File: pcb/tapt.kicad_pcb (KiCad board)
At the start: 4 copper layers, 28.3 x 28.3 mm, 38 parts, among them J1 Conn_01x05_Pin, J2 Conn_01x04_MountingPin, SW1 SW_SPDT_LIMIT, SW2 SW_SPST, U1 nRF52810-QCxx, Y1 32MHz, Y2 32.768kHz

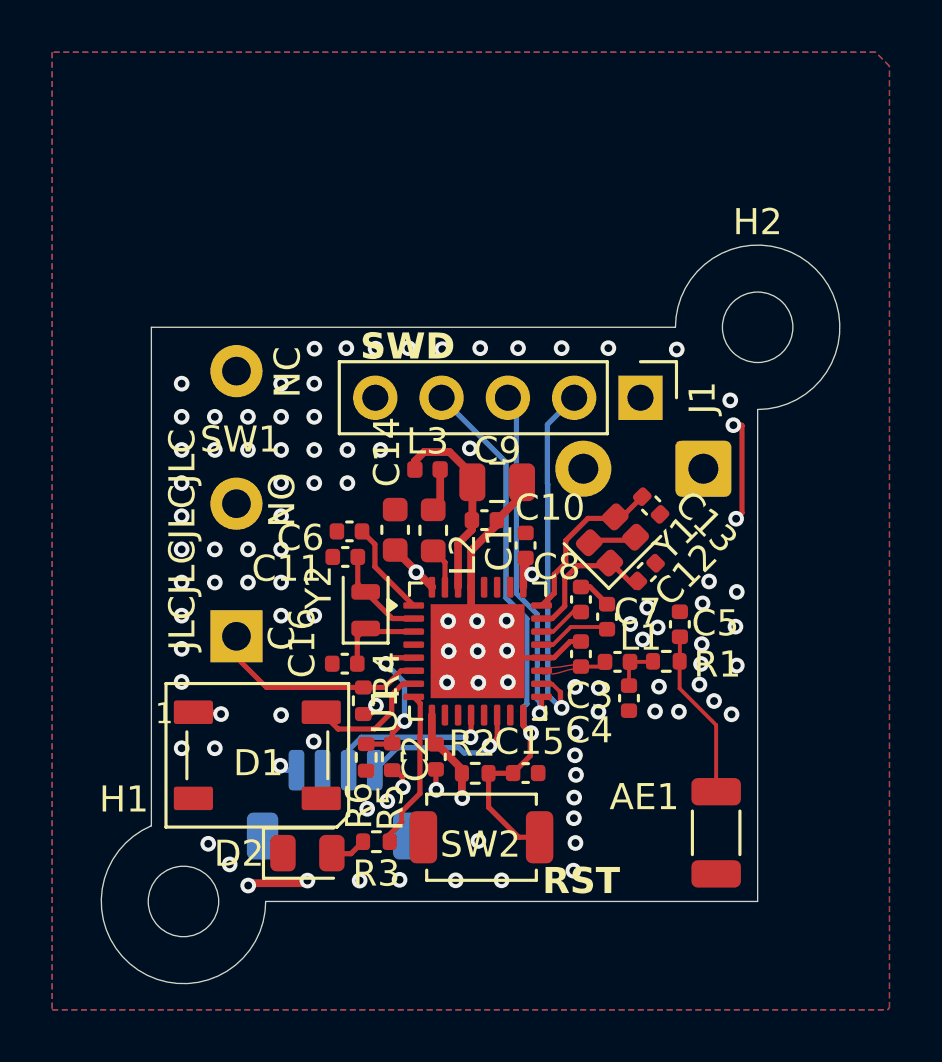
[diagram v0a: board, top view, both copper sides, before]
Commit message: pcb: voltage divider, antenna t-network
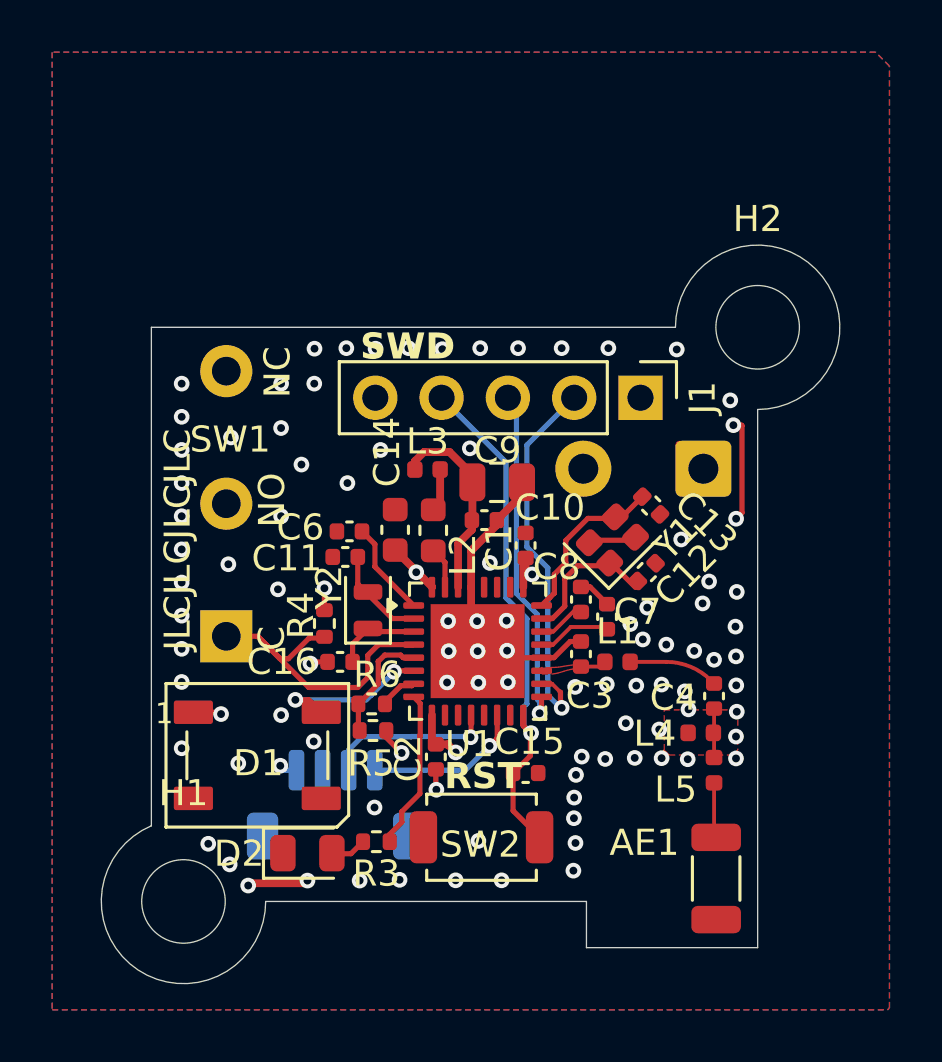
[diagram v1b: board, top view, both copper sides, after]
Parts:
- removed C5: 1pF, Capacitor_SMD:C_0402_1005Metric
- removed R1: 0, Resistor_SMD:R_0402_1005Metric
- removed R2: 100k, Resistor_SMD:R_0402_1005Metric
- added L4: 2.7nH, Inductor_SMD:L_0402_1005Metric, F.Cu at (106.7, 76.0)
- added L5: 3.9nH, Inductor_SMD:L_0402_1005Metric, F.Cu at (107.2, 77.4)
- C4: value 1pF -> 1.0pF
- H1, H2: footprint MountingHole:MountingHole_2.7mm_M2.5 -> MountingHole:MountingHole_3.2mm_M3
- L1: footprint Capacitor_SMD:C_0402_1005Metric -> Inductor_SMD:L_0402_1005Metric
- moved R4 3.31 mm to (92.2, 71.8), turned to 90 degrees
- moved C4 3.26 mm to (107.2, 74.6)
- moved R6 2.06 mm to (94.0, 74.9), turned to 0 degrees
- moved AE1 1.75 mm to (107.2, 81.6)
- moved R5 1.25 mm to (94.1, 75.9), turned to 180 degrees
- moved SW1 0.39 mm to (88.5, 72.3)
- moved C16 0.19 mm to (92.8, 73.3)
- moved Y2 0.09 mm to (93.9, 71.3)
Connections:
- C4 pad 2: GND -> Net-(C4-Pad2)
- R6 pad 2: GND -> BAT_MEASURE_GND
- U1 pad 4: unconnected-(U1-P0.04/AIN2-Pad4) -> LIMIT
- U1 pad 6: LIMIT -> NEOPIXEL
- U1 pad 7: NEOPIXEL -> BAT_MEASURE_GND
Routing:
- net Net-(AE1-FEED): track 6.50 -> 2.12 mm
- net LIMIT: track 8.34 -> 12.4 mm
- net Net-(C4-Pad2): track 0.00 -> 1.88 mm
- net RST: track 22.4 -> 20.7 mm
- net Net-(C4-Pad1): track 1.73 -> 3.44 mm
- net BAT_MEASURE_GND: track 0.00 -> 1.47 mm
- net NEOPIXEL: track 4.91 -> 6.20 mm, vias 0 -> 2
- net BAT_MEASURE: track 5.72 -> 4.48 mm, vias 2 -> 0
- net VDD: track 12.0 -> 10.9 mm
- net GND: track 21.1 -> 21.8 mm, vias 100 -> 94
- net SWDIO: track 14.0 -> 14.7 mm
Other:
- outline, holes or cut-outs redrawn

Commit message: pcb: minor rf routing improvements
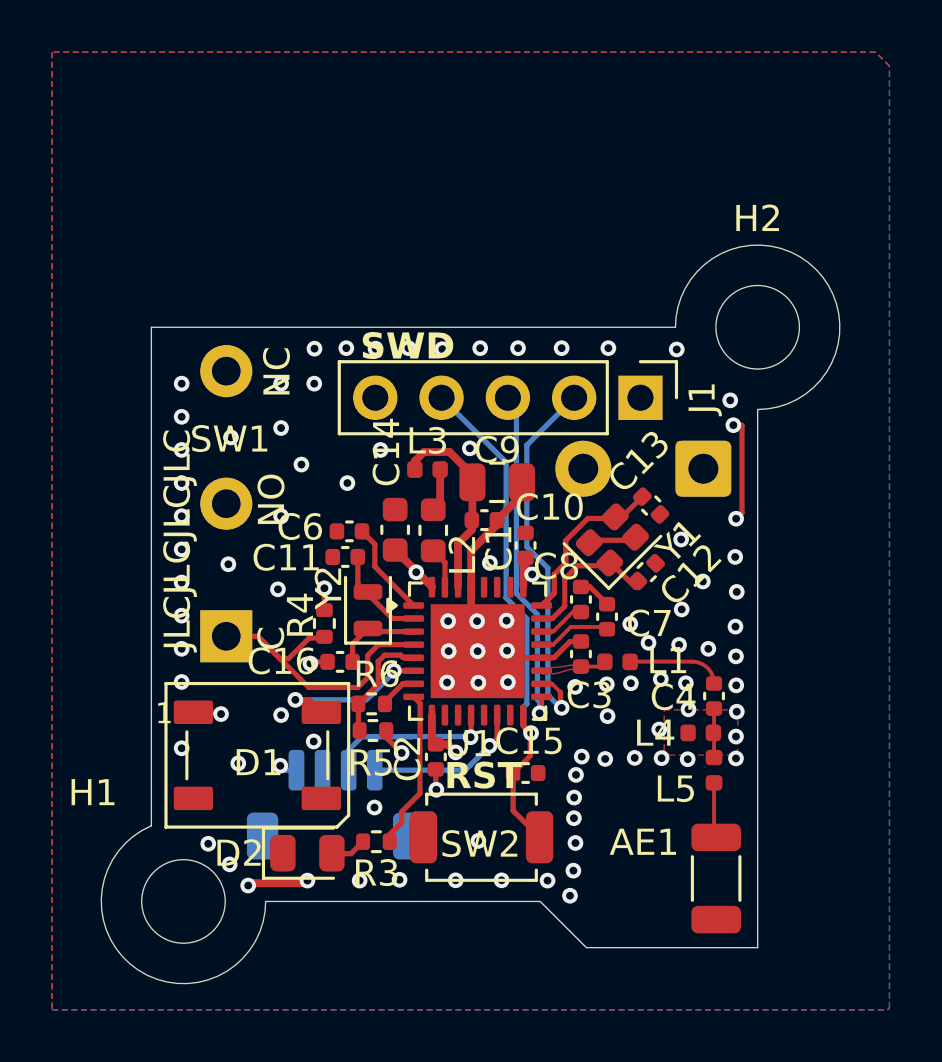
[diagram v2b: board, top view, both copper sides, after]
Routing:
- net GND: vias 94 -> 95
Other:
- outline, holes or cut-outs redrawn
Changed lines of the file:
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@@
 		(tags "capacitor")
 		(property "Reference" "C13"
-			(at -1.937473 1.046518 135)
+			(at 1.513209 0.86267 225)
 			(layer "F.SilkS")
 			(effects
@@
 		(tags "capacitor")
 		(property "Reference" "C7"
-			(at -0.19 -1.17 0)
+			(at 0.28 -1.64 0)
 			(layer "F.SilkS")
 			(effects
@@
 		(tags "inductor")
 		(property "Reference" "L1"
-			(at 0 -1.17 0)
+			(at 1.94 -0.03 0)
 			(layer "F.SilkS")
 			(effects
@@
 		(tags "mountinghole M3")
 		(property "Reference" "H1"
-			(at 0 -4.15 0)
+			(at -3.47 -4.15 0)
 			(layer "F.SilkS")
 			(effects
@@
 		(descr "SMD2016/4, Crystal, 2.0x1.6mm package, SMD, generated with kicad-footprint-generator make_crystal.py, http://www.q-crystal.com/upload/5/2015552223166229.pdf")
 		(property "Reference" "Y1"
-			(at 1.781945 1.674299 45)
+			(at 1.784691 1.841259 45)
 			(layer "F.SilkS")
 			(effects
@@
 		(tags "capacitor")
 		(property "Reference" "C12"
-			(at -0.989949 -1.131371 225)
+			(at -1.1243 -1.265721 225)
 			(layer "F.SilkS")
 			(effects
@@
 	)
 	(gr_line
-		(start 102.27 82.46)
+		(start 100.5 82.46)
 		(end 89.979937 82.46)
 		(stroke
@@
 	)
 	(gr_line
-		(start 102.27 82.46)
+		(start 100.5 82.46)
 		(end 102.27 84.23)
 		(stroke
@@
 	)
 	(via
-		(at 107.16 73.2)
-		(size 0.6)
-		(drill 0.3)
-		(layers "F.Cu" "B.Cu")
-		(free yes)
-		(net 3)
-	)
-	(via
 		(at 98.1 72.87)
 		(size 0.6)
@@
 	)
 	(via
-		(at 106.4 72.86)
-		(size 0.6)
-		(drill 0.3)
-		(layers "F.Cu" "B.Cu")
-		(free yes)
-		(net 3)
-	)
-	(via
-		(at 104.6 71.2)
+		(at 105.92 71.27)
 		(size 0.6)
 		(drill 0.3)
@@
 	)
 	(via
+		(at 101.64 82.24)
+		(size 0.6)
+		(drill 0.3)
+		(layers "F.Cu" "B.Cu")
+		(free yes)
+		(net 3)
+	)
+	(via
 		(at 86.76119 70.24)
 		(size 0.6)
@@
 	)
 	(via
+		(at 100.78 81.66)
+		(size 0.6)
+		(drill 0.3)
+		(layers "F.Cu" "B.Cu")
+		(free yes)
+		(net 3)
+	)
+	(via
 		(at 101.85 80.22)
 		(size 0.6)
@@
 	)
 	(via
+		(at 105.82 72.63)
+		(size 0.6)
+		(drill 0.3)
+		(layers "F.Cu" "B.Cu")
+		(free yes)
+		(net 3)
+	)
+	(via
 		(at 91.694265 73.344265)
 		(size 0.6)
@@
 	)
 	(via
-		(at 105.33 72.62)
-		(size 0.6)
-		(drill 0.3)
-		(layers "F.Cu" "B.Cu")
-		(free yes)
-		(net 3)
-	)
-	(via
 		(at 101.87 77.61)
 		(size 0.6)
@@
 	)
 	(via
-		(at 106.97 70.2)
+		(at 107.97 69.26)
 		(size 0.6)
 		(drill 0.3)
@@
 	)
 	(via
-		(at 106.04 74.41)
+		(at 106.08 74.1)
 		(size 0.6)
 		(drill 0.3)
@@
 	)
 	(via
-		(at 104.43 72.42)
+		(at 104.65 72.55)
 		(size 0.6)
 		(drill 0.3)
@@
 	)
 	(via
-		(at 103.78 75.63)
+		(at 103.08 75.36)
 		(size 0.6)
 		(drill 0.3)
@@
 	)
 	(via
-		(at 104.18 74.19)
+		(at 103.972917 74.1)
 		(size 0.6)
 		(drill 0.3)
@@
 	)
 	(via
-		(at 106.72 71.04)
+		(at 106.73 70.2)
 		(size 0.6)
 		(drill 0.3)
@@
 	)
 	(via
+		(at 106.94 72.78)
+		(size 0.6)
+		(drill 0.3)
+		(layers "F.Cu" "B.Cu")
+		(free yes)
+		(net 3)
+	)
+	(via
 		(at 108.01 74.18)
 		(size 0.6)
@@
 	)
 	(via
-		(at 105.15 74.15)
+		(at 105.12 73.94)
 		(size 0.6)
 		(drill 0.3)
@@
 	)
 	(segment
-		(start 105.33 73.28)
-		(end 103.945 73.28)
+		(start 103.945 73.28)
+		(end 103.955 73.27)
+		(width 0.1483)
+		(layer "F.Cu")
+		(net 6)
+	)
+	(segment
+		(start 107.16 74.11)
+		(end 107.16 74.11)
+		(width 0.1483)
+		(layer "F.Cu")
+		(net 6)
+	)
+	(segment
+		(start 106.32 73.27)
+		(end 103.955 73.27)
 		(width 0.1483)
 		(layer "F.Cu")
@@
 	)
 	(arc
-		(start 105.33 73.28)
-		(mid 106.253878 73.46377)
-		(end 107.037105 73.987106)
+		(start 107.16 74.11)
+		(mid 106.913969 73.51603)
+		(end 106.32 73.27)
 		(width 0.1483)
 		(layer "F.Cu")
@@
 	)
 	(segment
-		(start 95.65 73.62)
+		(start 94.928279 73.621)
 		(end 94.929279 73.62)
 		(width 0.2)
@@
 	)
 	(segment
+		(start 94.892 73.621)
+		(end 94.928279 73.621)
+		(width 0.2)
+		(layer "F.Cu")
+		(net 13)
+	)
+	(segment
 		(start 91.117573 74.735646)
 		(end 91.635646 74.735646)
@@
 	)
 	(segment
-		(start 91.635646 74.735646)
-		(end 92.11 75.21)
+		(start 94.929279 73.62)
+		(end 95.65 73.62)
 		(width 0.2)
 		(layer "F.Cu")
@@
 	)
 	(segment
-		(start 94.929279 73.62)
-		(end 94.891999 73.65728)
+		(start 91.635646 74.735646)
+		(end 92.11 75.21)
 		(width 0.2)
 		(layer "F.Cu")
@@
 	)
 	(via
-		(at 94.891999 73.65728)
+		(at 94.892 73.621)
 		(size 0.6)
 		(drill 0.3)
@@
 	)
 	(segment
-		(start 91.117573 74.735646)
-		(end 93.834536 74.735646)
+		(start 93.834536 74.735646)
+		(end 91.117573 74.735646)
 		(width 0.2)
 		(layer "B.Cu")
@@
 	(segment
 		(start 94.017616 74.56)
-		(end 94.891999 73.685617)
+		(end 94.010182 74.56)
 		(width 0.2)
 		(layer "B.Cu")
@@
 	)
 	(segment
-		(start 94.010182 74.56)
-		(end 94.017616 74.56)
+		(start 94.892 73.621)
+		(end 94.891999 73.621001)
 		(width 0.2)
 		(layer "B.Cu")
@@
 	(segment
 		(start 94.891999 73.685617)
-		(end 94.891999 73.65728)
+		(end 94.017616 74.56)
 		(width 0.2)
 		(layer "B.Cu")
@@
 	)
 	(segment
-		(start 93.834536 74.735646)
-		(end 94.010182 74.56)
+		(start 94.891999 73.621001)
+		(end 94.891999 73.685617)
+		(width 0.2)
+		(layer "B.Cu")
+		(net 13)
+	)
+	(segment
+		(start 94.010182 74.56)
+		(end 93.834536 74.735646)
 		(width 0.2)
 		(layer "B.Cu")
@@
 	)
 	(segment
-		(start 95.160202 74.194)
-		(end 95.576 74.194)
-		(width 0.2)
-		(layer "F.Cu")
-		(net 36)
-	)
-	(segment
 		(start 94.55 74.804202)
-		(end 95.160202 74.194)
+		(end 94.55 74.89)
 		(width 0.2)
 		(layer "F.Cu")
@@
 	)
 	(segment
-		(start 94.55 74.89)
+		(start 95.234202 74.12)
 		(end 94.55 74.804202)
 		(width 0.2)
@@
 	)
 	(segment
-		(start 95.576 74.194)
-		(end 95.65 74.12)
+		(start 95.65 74.12)
+		(end 95.234202 74.12)
 		(width 0.2)
 		(layer "F.Cu")

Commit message: chore: production files, bom, readme updates
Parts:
- moved L1 0.18 mm to (103.5, 73.1)
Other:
- board text added: "Stackup: JLC04161H-7628"
- board text removed: "Stackup: JLC04161H-3313"
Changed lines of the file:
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@@
 	(footprint "Inductor_SMD:L_0402_1005Metric"
 		(layer "F.Cu")
-		(at 103.46 73.28)
+		(at 103.46 73.1)
 		(descr "Inductor SMD 0402 (1005 Metric), square (rectangular) end terminal, IPC-7351 nominal, (Body size source: http://www.tortai-tech.com/upload/download/2011102023233369053.pdf), generated with kicad-footprint-generator")
 		(tags "inductor")
@@
 		)
 	)
-	(gr_text "Stackup: JLC04161H-3313"
+	(gr_text "Stackup: JLC04161H-7628"
 		(at 81.56 48.77 0)
 		(layer "Cmts.User")
@@
 	)
 	(segment
-		(start 107.24 80.005)
+		(start 107.16 77.915)
 		(end 107.16 79.925)
-		(width 0.1483)
+		(width 0.2939)
 		(layer "F.Cu")
 		(net 1)
@@
 	(segment
 		(start 107.16 79.925)
-		(end 107.16 77.915)
-		(width 0.1483)
+		(end 107.24 80.005)
+		(width 0.2939)
 		(layer "F.Cu")
 		(net 1)
@@
 	)
 	(via
-		(at 100.78 81.66)
+		(at 107.01 72.59)
 		(size 0.6)
 		(drill 0.3)
@@
 	)
 	(via
-		(at 101.85 80.22)
+		(at 106.04 72.39)
 		(size 0.6)
 		(drill 0.3)
@@
 	)
 	(via
-		(at 95.11 81.63)
+		(at 100.78 81.66)
 		(size 0.6)
 		(drill 0.3)
@@
 	)
 	(via
-		(at 90.57 64.32)
+		(at 101.85 80.22)
 		(size 0.6)
 		(drill 0.3)
@@
 	)
 	(via
-		(at 102.99 77)
+		(at 95.11 81.63)
 		(size 0.6)
 		(drill 0.3)
@@
 	)
 	(via
-		(at 105.82 72.63)
+		(at 90.57 64.32)
+		(size 0.6)
+		(drill 0.3)
+		(layers "F.Cu" "B.Cu")
+		(free yes)
+		(net 3)
+	)
+	(via
+		(at 102.99 77)
 		(size 0.6)
 		(drill 0.3)
@@
 	)
 	(via
-		(at 106.08 74.1)
+		(at 106.29 74.16)
 		(size 0.6)
 		(drill 0.3)
@@
 	)
 	(via
-		(at 104.65 72.55)
-		(size 0.6)
-		(drill 0.3)
-		(layers "F.Cu" "B.Cu")
-		(free yes)
-		(net 3)
-	)
-	(via
 		(at 108.03 70.6)
 		(size 0.6)
@@
 	)
 	(via
+		(at 104.61 72.34305)
+		(size 0.6)
+		(drill 0.3)
+		(layers "F.Cu" "B.Cu")
+		(free yes)
+		(net 3)
+	)
+	(via
 		(at 96.93 74.07)
 		(size 0.6)
@@
 	)
 	(via
-		(at 103.972917 74.1)
+		(at 104.334123 73.876328)
 		(size 0.6)
 		(drill 0.3)
@@
 	)
 	(via
-		(at 106.94 72.78)
-		(size 0.6)
-		(drill 0.3)
-		(layers "F.Cu" "B.Cu")
-		(free yes)
-		(net 3)
-	)
-	(via
 		(at 108.01 74.18)
 		(size 0.6)
@@
 	)
 	(via
-		(at 103.05 74.14)
+		(at 102.99 73.92)
 		(size 0.6)
 		(drill 0.3)
@@
 	)
 	(via
-		(at 105.12 73.94)
+		(at 105.46 73.63695)
 		(size 0.6)
 		(drill 0.3)
@@
 	)
 	(segment
+		(start 102.19 73.46)
+		(end 102.55 73.1)
+		(width 0.2939)
+		(layer "F.Cu")
+		(net 5)
+	)
+	(segment
 		(start 102.06 73.46)
-		(end 102.8 73.46)
-		(width 0.1483)
+		(end 102.19 73.46)
+		(width 0.2939)
+		(layer "F.Cu")
+		(net 5)
+	)
+	(segment
+		(start 102.55 73.1)
+		(end 102.975 73.1)
+		(width 0.2939)
 		(layer "F.Cu")
 		(net 5)
@@
 	)
 	(segment
-		(start 103.945 73.28)
-		(end 103.955 73.27)
+		(start 107.16 74.11)
+		(end 107.16 74.11)
 		(width 0.1483)
 		(layer "F.Cu")
@@
 		(start 107.16 74.11)
 		(end 107.16 74.11)
-		(width 0.1483)
+		(width 0.2939)
 		(layer "F.Cu")
 		(net 6)
 	)
 	(segment
-		(start 106.32 73.27)
-		(end 103.955 73.27)
-		(width 0.1483)
+		(start 104.045 73.18)
+		(end 104.235 72.99)
+		(width 0.2939)
+		(layer "F.Cu")
+		(net 6)
+	)
+	(segment
+		(start 106.04 72.99)
+		(end 104.235 72.99)
+		(width 0.2939)
 		(layer "F.Cu")
 		(net 6)
 	)
 	(arc
-		(start 107.16 74.11)
-		(mid 106.913969 73.51603)
-		(end 106.32 73.27)
-		(width 0.1483)
+		(start 106.04 72.99)
+		(mid 106.831959 73.31804)
+		(end 107.16 74.11)
+		(width 0.2939)
 		(layer "F.Cu")
 		(net 6)
@@
 		(start 107.16 76.945)
 		(end 107.16 75.07)
-		(width 0.1483)
+		(width 0.2939)
 		(layer "F.Cu")
 		(net 37)
